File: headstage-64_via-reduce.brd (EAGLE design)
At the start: 23.4 x 25.8 mm, 195 parts, among them J8 DF40C-70DP-0.4V(51), J9 PINHD-1X5_HALF_CONNETOR, U1 ADA4062-4ACPZ-R7, U10 BNO055, U11 TS4231, U12 TS4231, U13 TLV70733, U14 10M08DC, U15 TLV70733, U16 LT3463, U17 TLV70725, U18 TPS62621, U19 ASCO-50.000MHZ-EK-T3, U2 AD5681RBCPZ-1RL7, U20 TLV70712, U3 CAT4016_QFN, U4 TPL0501_UQFN, U5 DG509B, U6 TS4231, U7 RHD2064_BGA, U8 TS4231, U9 DS90UB913A_WQFN

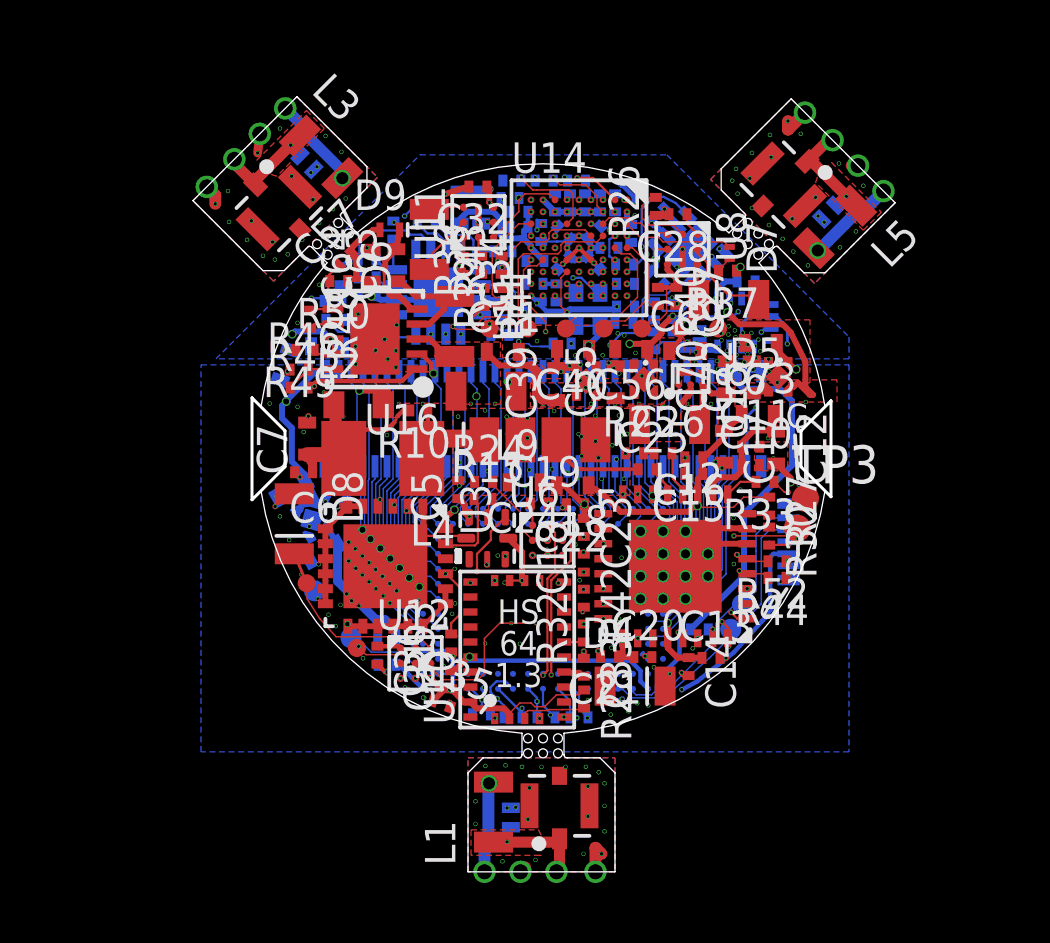
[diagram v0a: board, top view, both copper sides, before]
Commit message: onix-headstage-64 rev. 1.3B
- This is a patch ("B") on rev. 1.3, the beta-test version, that addresses
difficulties with assembly and use
- Assembly differences:
    - R45 has been adjusted right by 0.2 mm
    - C75-77 have been added to address noise leaking from vcoax into
    electrodes.
    - The adapter boards have been removed from the design. This results
    in non-contiguous reference designators, but components names have
    NOT been changed
- Copper pours have been added to all layers to aid with ease of pcb fab
and improve thermal performance
- Thermal reliefs have been added to contacts onto copper pours except
those where head dissipation is critical (power supplies)
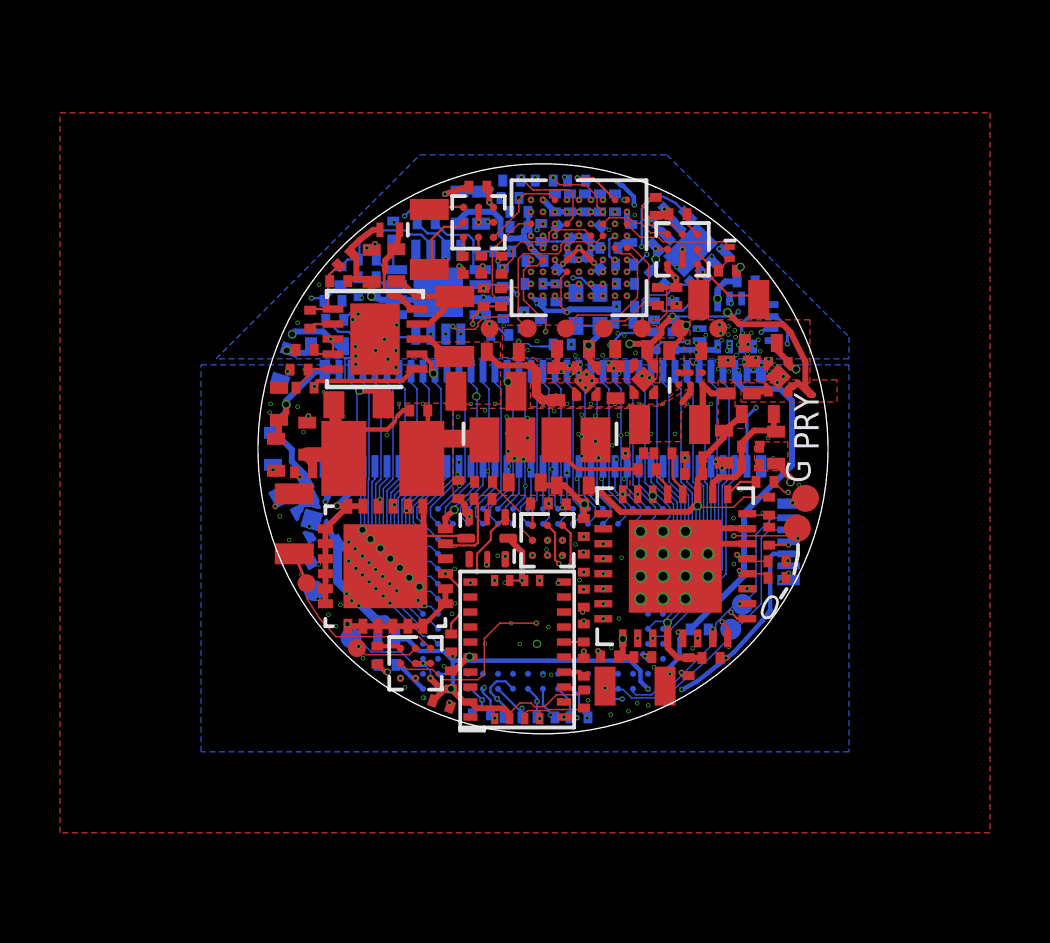
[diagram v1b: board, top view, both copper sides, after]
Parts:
- removed D1, D2, D3: SESD0402X1UN-0020-090, jonnew:0402T-DFN
- removed J1, J3, J6: (no value), jonnew:X_FL_R_SMT_1(02)
- removed J2, J4, J7: (no value), jonnew:HEADSTAGE64-DAUGHER-CARD-CASTELLATED
- removed L1, L3, L5: CIG21L4R7MNE, jonnew:0805T
- removed R20, R3, R9: 1k, jonnew:0201T
- added C74, C75, C77: 10uF, jonnew:0402T
- J9: value PINHD-1X5_HALF_CONNETOR -> (none)
- U9: value DS90UB913A_WQFN -> (none)
- moved R45 0.20 mm to (-7.93, 2.04)
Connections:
- removed net GND1: D2.A, J3.P$2, J3.P$3, J3.P$4, J4.2, J4.4
- removed net GND2: D1.A, J1.P$2, J1.P$3, J1.P$4, J2.2, J2.4
- removed net GND3: D3.A, J6.P$2, J6.P$3, J6.P$4, J7.2, J7.4
- removed net N$25: J4.1, L3.2, R9.2
- removed net N$48: J2.1, L1.2, R3.2
- removed net N$50: J7.1, L5.2, R20.2
- removed net _SIGOUT: D2.C, J3.P$1, J4.3, L3.1, R9.1
- removed net _SIGOUT1: D1.C, J1.P$1, J2.3, L1.1, R3.1
- removed net _SIGOUT2: D3.C, J6.P$1, J7.3, L5.1, R20.1
- net GND: now also C74.2, C75.2, C77.2
- net VCOAX: now also C74.1, C75.1, C77.1
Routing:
- net _SIGOUT: track 4.72 -> 0.00 mm, vias 1 -> 0
- net _SIGOUT1: track 4.31 -> 0.00 mm, vias 1 -> 0
- net GND: track 31.0 -> 35.3 mm, vias 205 -> 207
- net _SIGOUT2: track 4.26 -> 0.00 mm, vias 1 -> 0
- net N$48: track 3.44 -> 0.00 mm, vias 1 -> 0
- net N$50: track 3.44 -> 0.00 mm, vias 1 -> 0
- net N$25: track 3.11 -> 0.00 mm, vias 1 -> 0
- net +3V3: track 32.9 -> 36.0 mm, vias 26 -> 27
- net GND2: track 1.99 -> 0.00 mm, vias 22 -> 0
- net GND3: track 1.99 -> 0.00 mm, vias 22 -> 0
- net VCOAX: track 28.4 -> 30.0 mm
- net GND1: track 1.32 -> 0.00 mm, vias 22 -> 0
- net N$4: track 9.93 -> 10.1 mm, vias 2 -> 3
- net N$5: track 7.66 -> 7.74 mm, vias 2 -> 3
- added copper zone on layer 5, net +3V3
- added copper zone on layer 3, net GND
- added copper zone on layer 5, net GND
- added copper zone on layer 3, net N$4
- added copper zone on layer 5, net N$41
- added copper zone on layer 3, net N$5
- removed copper zone on layer 1, net GND1
- removed copper zone on layer 16, net GND1
- removed copper zone on layer 4, net GND1
- removed copper zone on layer 7, net GND1
- removed copper zone on layer 1, net GND2
- removed copper zone on layer 16, net GND2
- removed copper zone on layer 4, net GND2
- removed copper zone on layer 7, net GND2
- removed copper zone on layer 1, net GND3
- removed copper zone on layer 16, net GND3
- removed copper zone on layer 4, net GND3
- removed copper zone on layer 7, net GND3
- removed copper zone on layer 16, net N$25
- removed copper zone on layer 3, net N$41
- removed copper zone on layer 1, net N$43
- removed copper zone on layer 4, net N$43
- removed copper zone on layer 1, net N$48
- removed copper zone on layer 16, net N$48
- removed copper zone on layer 1, net N$49
- removed copper zone on layer 4, net N$49
- removed copper zone on layer 1, net N$50
- removed copper zone on layer 16, net N$50
- removed copper zone on layer 1, net N$51
- removed copper zone on layer 4, net N$51
- removed copper zone on layer 1, net _SIGOUT
- removed copper zone on layer 16, net _SIGOUT
- removed copper zone on layer 1, net _SIGOUT1
- removed copper zone on layer 16, net _SIGOUT1
- removed copper zone on layer 1, net _SIGOUT2
- removed copper zone on layer 16, net _SIGOUT2
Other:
- board size 23.4 x 25.8 mm -> 19 x 19 mm
- board text added: "HS-64 Rev.B"
- board text added: "PRY"
- board text removed: "(C) JPN&JV, MIT 2018 CERN OHL v.1.2"
- board text removed: "HS 64 1.3"
- board text removed: "HS-64 JPN JV"
- board text removed: "HS-64 Rev1.3"
